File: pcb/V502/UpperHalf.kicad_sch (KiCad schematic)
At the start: 28 parts, among them U1 74LS670, U10 74LS157, U11 74LS157, U12 74LS157, U2 74LS670, U3 74LS670, U4 74LS670, U5 74LS283, U6 74LS283, U7 74LS283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

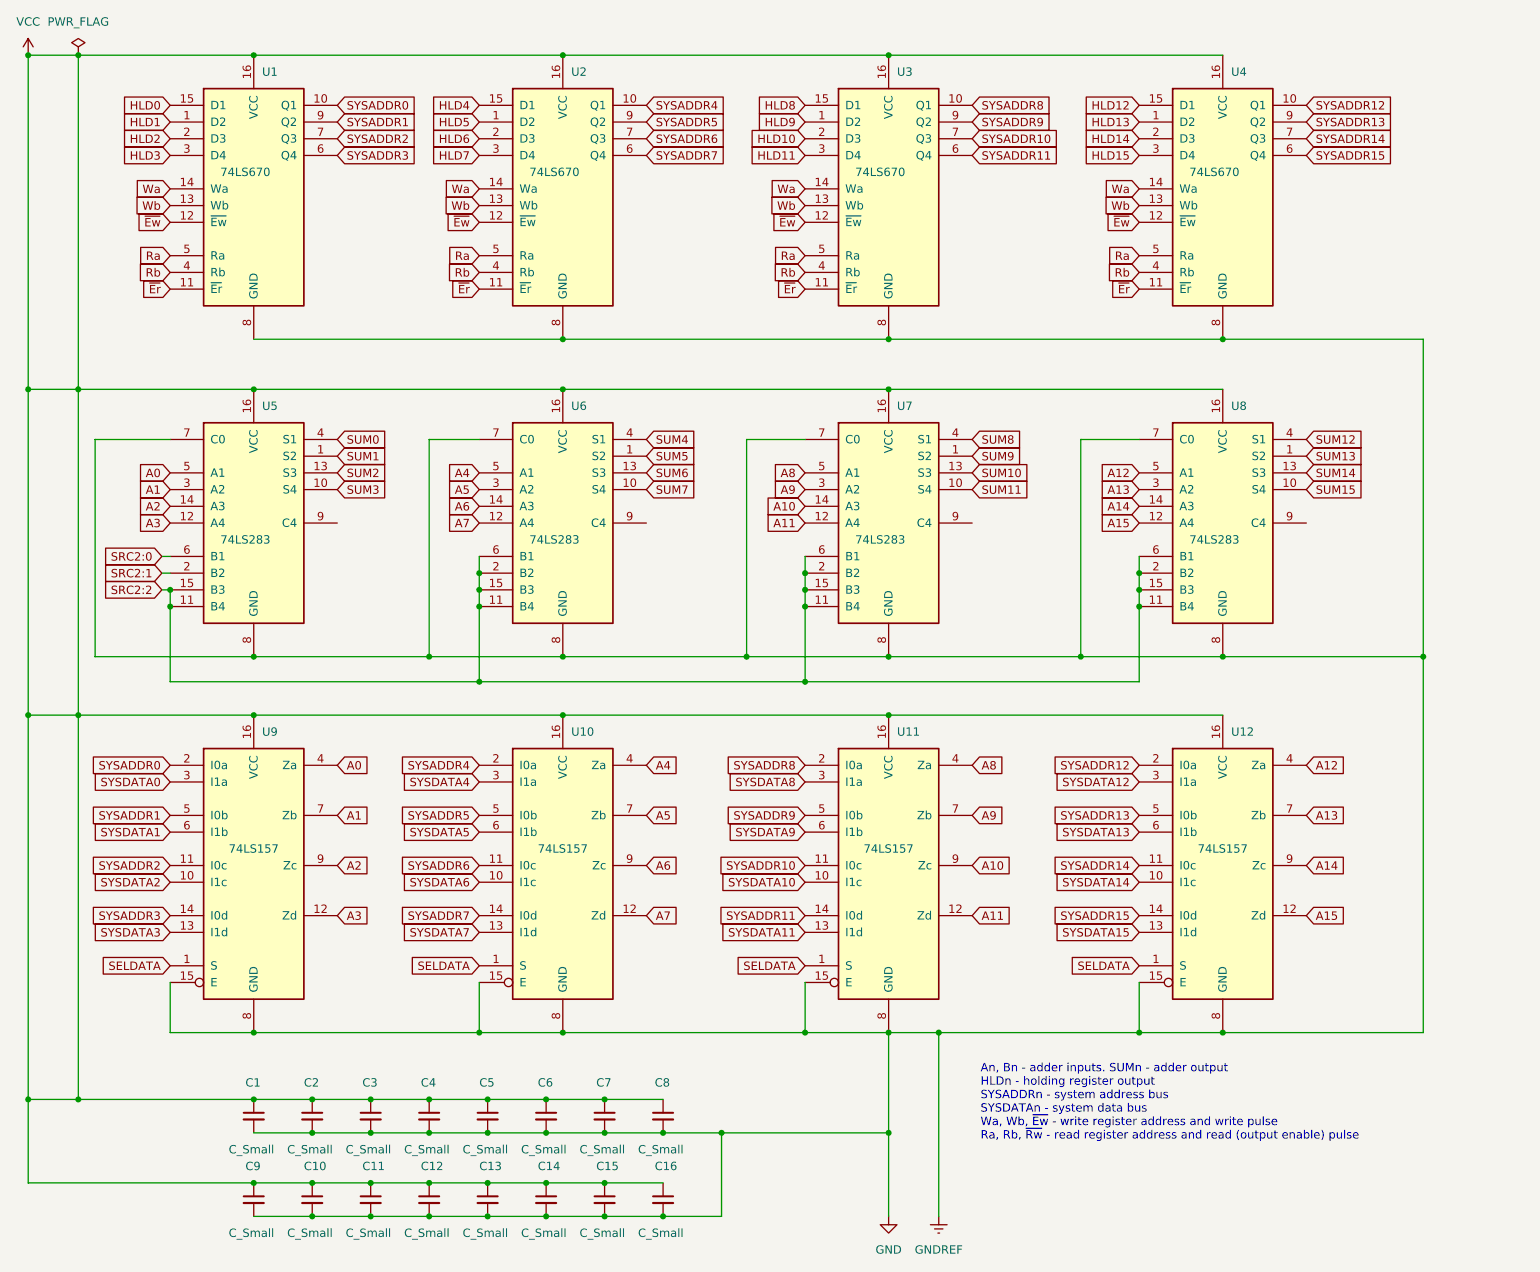
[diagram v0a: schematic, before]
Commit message: V502 board almost completely routed.
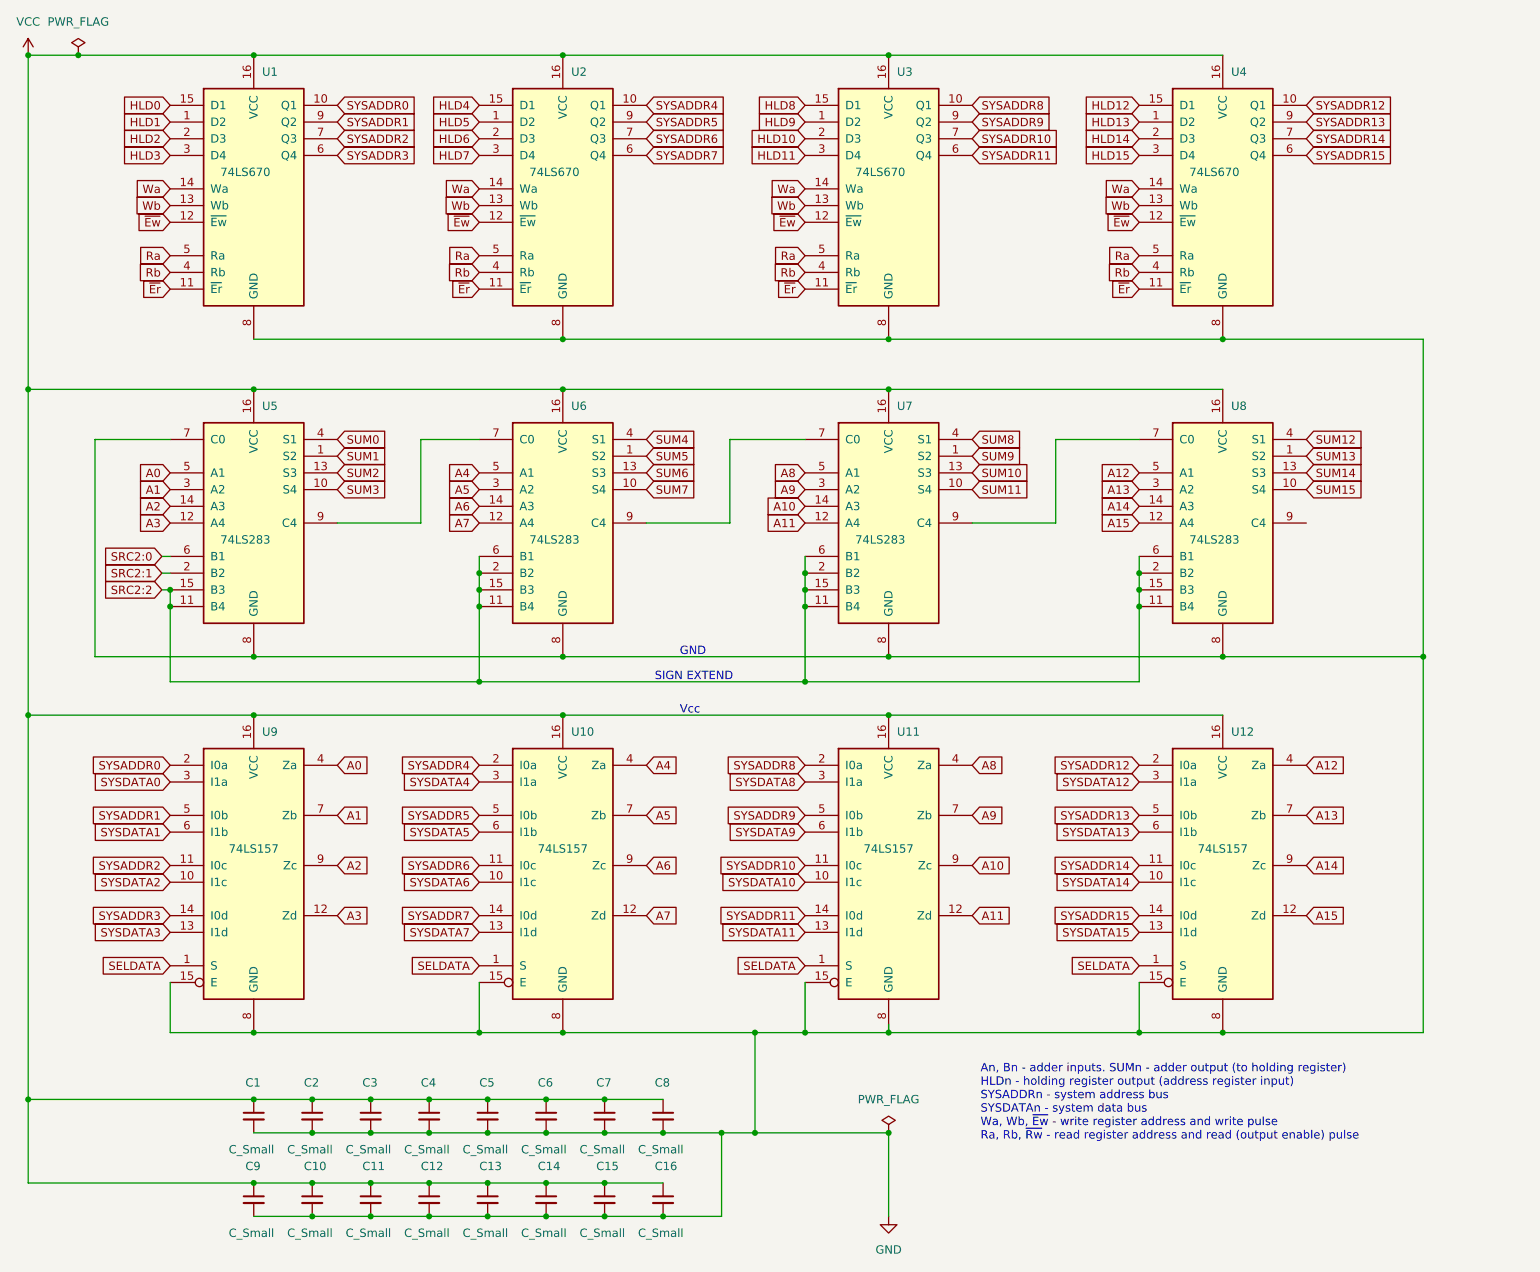
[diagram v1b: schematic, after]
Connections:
- net GND: no longer U6.7 (C0), U7.7 (C0), U8.7 (C0)
- net at U5.9 (C4): now also U6.7 (C0)
- net at U7.9 (C4): now also U8.7 (C0)
- net at U6.9 (C4): now also U7.7 (C0)
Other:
- note added: "An, Bn - adder inputs. SUMn - adder output (to holding register) HLDn - holding register output (address register input) SYSADDRn - system address bus SYSDATAn - system data bus Wa, Wb, ~{Ew} - write register address and write pulse Ra, Rb, ~{Rw} - read register address and read (output enable) pulse"
- note added: "GND"
- note added: "SIGN EXTEND"
- note added: "Vcc"
- note removed: "An, Bn - adder inputs. SUMn - adder output HLDn - holding register output SYSADDRn - system address bus SYSDATAn - system data bus Wa, Wb, ~{Ew} - write register address and write pulse Ra, Rb, ~{Rw} - read register address and read (output enable) pulse"
